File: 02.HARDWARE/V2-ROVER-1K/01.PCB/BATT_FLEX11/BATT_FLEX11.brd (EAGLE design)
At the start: 11.7 x 28.2 mm, 4 parts, among them K3 FLEX11, K4 FLEX11, K7 FLEX11, K8 FLEX11

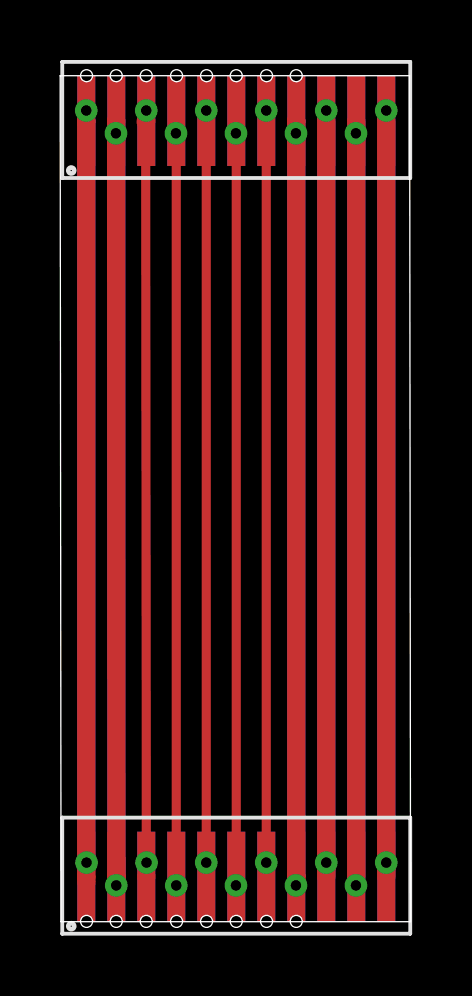
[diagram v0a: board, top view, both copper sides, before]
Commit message: Ajuste de ancho de pista para lineas de potencias.
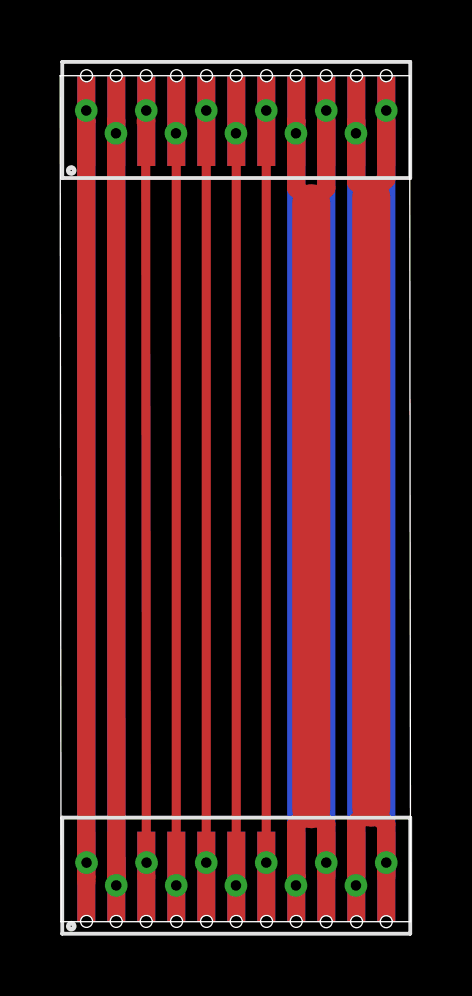
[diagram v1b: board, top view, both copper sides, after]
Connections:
- removed net F11-11: K3.12, K4.12, K7.12, K8.12
- removed net F11-9: K3.10, K4.10, K7.10, K8.10
- net F11-10: now also K3.12, K4.12, K7.12, K8.12
- net F11-8: now also K3.10, K4.10, K7.10, K8.10
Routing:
- net F11-9: track 50.4 -> 0.00 mm
- net F11-11: track 50.4 -> 0.00 mm
- net F11-8: track 50.7 -> 81.4 mm
- net F11-10: track 50.4 -> 81.1 mm
